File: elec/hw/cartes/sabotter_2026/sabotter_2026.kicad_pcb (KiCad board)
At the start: 2 copper layers, 105 x 80 mm, 131 parts, among them J10 2-1445055-3, J11 3-794618-6, J12 22053031, J13 3-794618-6, J3 USB4105-GF-A-060, J5 2-1445055-4, J6 794618-4, J7 A3C-16DA-2DSC71, J8 A3C-16DA-2DSC71, J9 794618-4, SW1 TSB001A3526A02, U1 OKI-78SR-3.3/1.5-W36H-C, U2 OKI-78SR-5/1.5-W36H-C, U3 ESP32-S3-WROOM-1, U4 ADXRS453BRGZ, U5 SCH16T-K01-10, U6 TCAN1042DRQ1, U7 TCA6408ARGTR, U8 SN74LVC1T45DBV

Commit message: switchs added to motor ribbon cable
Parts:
- added R59: 0R, cocotter_resistor:r0603_reflow, F.Cu at (88.2, -19.9)
- added R60: 0R, cocotter_resistor:r0603_reflow, F.Cu at (88.2, -17.5)

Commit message: sabotter wip
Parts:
- removed C11, C13, C14, C18, C20: 1µF 50V, cocotter_capacitors:C_0805_2012Metric
- removed C15, C16, C19: 100nF 50V, cocotter_capacitors:C_0603_1608Metric
- removed C17: 10µF 25V, cocotter_capacitors:C_0805_2012Metric
- removed D5: 1N5819WS, cocotter_diodes:D_SOD-323
- removed H5: MOUNT-PAD-ROUND3.3, cocotter_others:MountingHole_3.2mm_M3_Pad_Via
- removed J7, J8: A3C-16DA-2DSC71, cocotter_connectors:A3C-16DA-2DSC71
- removed L1: 470µH, cocotter_inductors:L_Kyocera_07A7_7.3x6.6mm
- removed R27: 100k, cocotter_resistor:r0603_reflow
- removed R35, R36: 91k 1%, cocotter_resistor:r0603_reflow
- removed R37, R38: 0R, cocotter_resistor:r0603_reflow
- removed TP4, TP5: TestPoint, cocotter_others:testpoint-THT-0.5mm
- removed U4: ADXRS453BRGZ, cocotter_ic:SOIC-16W_7.5x10.3mm_P1.27mm
- removed U5: SCH16T-K01-10, cocotter_ic:SCH16T
- added C30: 100nF 50V, cocotter_capacitors:C_0603_1608Metric, F.Cu at (149.8, 55.8)
- added J17: 22272061, cocotter_connectors:22272061, B.Cu at (150.0, 50.5)
- added J18: ~, cocotter_connectors:188275-4, B.Cu at (124.8, 88.0)
- added R61: 0R, cocotter_resistor:r0603_reflow, F.Cu at (143.8, 55.8)
- added R62: 91k 1%, cocotter_resistor:r0603_reflow, F.Cu at (157.5, 97.5)
- added R63: 91k 1%, cocotter_resistor:r0603_reflow, F.Cu at (154.4, 97.5)
- added R64: 91k 1%, cocotter_resistor:r0603_reflow, F.Cu at (144.8, 48.0)
- added R65: 0R, cocotter_resistor:r0603_reflow, F.Cu at (167.2, 67.5)
- added TP7: TestPoint, cocotter_others:testpoint-THT-0.5mm, F.Cu at (151.8, 54.5)
- added TP8: TestPoint, cocotter_others:testpoint-THT-0.5mm, F.Cu at (151.8, 56.5)
- added U9: ~, cocotter_ic:OLED_0.96inch, F.Cu at (150.0, 72.0)
- J1: value ~ -> 22272021; moved to B.Cu
- J10: value 2-1445055-3 -> 2-1445051-3; footprint cocotter_connectors:2-1445055-3 -> cocotter_connectors:2-1445051-3; moved to B.Cu
- J11: value 3-794618-6 -> 22272051; footprint cocotter_connectors:3-794618-6 -> cocotter_connectors:22272051; moved to B.Cu
- J12: value 22053031 -> 22272031; footprint cocotter_connectors:22053031 -> cocotter_connectors:22272031; moved to B.Cu
- J13: value 3-794618-6 -> 3-794630-6; footprint cocotter_connectors:3-794618-6 -> cocotter_connectors:3-794630-6; moved to B.Cu
- J15, J16, J4: moved to B.Cu
- J3: value USB4105-GF-A-060 -> USB4120-03-C; footprint cocotter_connectors:USB4105 -> cocotter_connectors:USB4120-03-C
- J5: value 2-1445055-4 -> 22272041; footprint cocotter_connectors:2-1445055-4 -> cocotter_connectors:22272041; moved to B.Cu
- J6, J9: value 794618-4 -> 3-794630-4; footprint cocotter_connectors:798618-4 -> cocotter_connectors:3-794630-4; moved to B.Cu
- R54: value 91k 1% -> 0R
- R55: value 0R -> 91k 1%
- R57: value 91k 1% -> 1k 1%
- R58: value 1k 1% -> 0R
- SW1: value TSB001A3526A02 -> PTS525 SK15 SMTR2 LFS; footprint cocotter_others:TSB001A3526A02 -> cocotter_others:PTS525 SK15 SMTR2 LFS
- moved C25 229.9 mm to (173.0, 108.0), turned to -90 degrees
- moved C26 225.4 mm to (168.5, 108.0), turned to -90 degrees
- moved TP6 217.4 mm to (170.0, 96.5)
- moved U7 213.5 mm to (166.1, 94.8)
- moved R55 208.6 mm to (114.0, 109.0), turned to 180 degrees
- moved R56 203.1 mm to (117.0, 104.5)
- moved U8 199.3 mm to (118.0, 107.0)
- moved R49 185.1 mm to (171.5, 108.0), turned to 90 degrees
- moved U6 184.7 mm to (138.8, 95.9)
- moved R12 176.7 mm to (154.8, 56.5), turned to 180 degrees
- moved C1 174.1 mm to (115.0, 78.0), turned to -90 degrees
- moved R54 172.1 mm to (127.8, 100.2), turned to -90 degrees
- moved R9 170.7 mm to (150.8, 95.0), turned to 180 degrees
- moved R5 168.5 mm to (150.8, 97.0), turned to 180 degrees
- moved R10 167.8 mm to (147.8, 95.0), turned to 180 degrees
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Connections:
- net /motors/MOSI_MOT_3V3 renamed /motors/irq1_3v3
- J11 pad 2: +3V3 -> /interfaces/scl_3v3
- J11 pad 3: /interfaces/scl_3v3 -> /interfaces/sda_3v3
- J11 pad 4: Net-(J11-Pad4) -> +3V3
- J11 pad 5: /interfaces/sda_3v3 -> Net-(J11-Pad5)
- J13 pad 2: +3V3 -> /scl_tof_3v3
- J13 pad 3: /uc/scl_tof_3v3 -> /sda_tof_3v3
- J13 pad 4: /interfaces/enable_tof_3v3 -> +3V3
- J13 pad 5: /uc/sda_tof_3v3 -> /interfaces/enable_tof_3v3
- J14 pad 13: /motors/MISO_MOT_3V3 -> /motors/irq0_3v3
- J14 pad 15: /motors/SCK_MOT_3V3 -> /sda_tof_3v3
- J14 pad 16: /motors//CS_MOT0_3V3 -> /scl_tof_3v3
- J15 pad 13: /motors/MISO_MOT_3V3 -> /motors/irq0_3v3
- J15 pad 15: /motors/SCK_MOT_3V3 -> /sda_tof_3v3
- J15 pad 16: /motors//CS_MOT1_3V3 -> /scl_tof_3v3
- J16 pad 13: /motors/MISO_MOT_3V3 -> /motors/irq0_3v3
- J16 pad 15: /motors/SCK_MOT_3V3 -> /sda_tof_3v3
- J16 pad 16: /motors//CS_MOT2_3V3 -> /scl_tof_3v3
- R10 pad 2: /uc/sda_tof_3v3 -> /sda_tof_3v3
- R50 pad 2: /interfaces/ctc_left_3v3 -> Net-(U7-~{RESET})
- R51 pad 2: Net-(U7-~{RESET}) -> /interfaces/ctc_left_3v3
- R54 pad 1: /interfaces/ws2812_data_3v3 -> +5V
- R54 pad 2: GND -> Net-(J11-Pad5)
- R55 pad 1: +3V3 -> /interfaces/ws2812_data_3v3
- R55 pad 2: Net-(U8-DIR) -> GND
- R56 pad 1: +5V -> +3V3
- R56 pad 2: Net-(J11-Pad6) -> Net-(U8-DIR)
- R57 pad 1: +3V3 -> /interfaces/led_com_3v3
- R57 pad 2: Net-(J11-Pad4) -> Net-(D6-PadA)
- R58 pad 1: /interfaces/led_com_3v3 -> GND
- R58 pad 2: Net-(D6-PadA) -> Net-(U9-GND)
- R59 pad 1: /motors/MISO_MOT_3V3 -> Net-(U9-VCC)
- R59 pad 2: /motors/ctc_right_3v3 -> GND
- R6 pad 2: /uc/scl_tof_3v3 -> /scl_tof_3v3
- R60 pad 1: /motors/SCK_MOT_3V3 -> Net-(U9-VCC)
- R60 pad 2: /motors/ctc_left_3v3 -> +3V3
- TP1 pad 1: /uc/sda_tof_3v3 -> /sda_tof_3v3
- TP2 pad 1: /uc/scl_tof_3v3 -> /scl_tof_3v3
- U3 pad 10: /uc/sda_tof_3v3 -> /sda_tof_3v3
- U3 pad 11: /uc/scl_tof_3v3 -> /scl_tof_3v3
- U6 pad 1: (no net) -> /interfaces/can_tx_3v3
- U7 pad 4: /interfaces/ctc_right_3v3 -> /interfaces/enable_tof_3v3
- U7 pad 5: /interfaces/ctc_left_3v3 -> /interfaces/reset_tof_3v3
- U7 pad 7: /interfaces/reset_tof_3v3 -> /brake_mot_3v3
- U7 pad 8: /interfaces/enable_tof_3v3 -> /interfaces/ctc_left_3v3
- U7 pad 9: /brake_mot_3v3 -> /interfaces/ctc_right_3v3
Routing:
- net /interfaces/scl_3v3: track 0.00 -> 82.9 mm, vias 0 -> 1
- net /interfaces/sda_3v3: track 0.00 -> 78.7 mm, vias 0 -> 2
- net GND: track 0.00 -> 71.9 mm, vias 0 -> 18
- net /uc/USB_D-: track 0.00 -> 51.1 mm, vias 0 -> 2
- net /uc/EN_ESP32_3v3: track 0.00 -> 46.8 mm, vias 0 -> 2
- net /uc/USB_D+: track 0.00 -> 46.8 mm, vias 0 -> 2
- net +3V3: track 0.00 -> 38.5 mm, vias 0 -> 9
- net /uc/esp32_dbg_tx_3v3: track 0.00 -> 36.6 mm
- net /uc/boot/dl_select_3v3: track 0.00 -> 30.9 mm
- net /interfaces/CAN_H: track 0.00 -> 29.8 mm
- net /sensors/lidar_tx_3v3: track 0.00 -> 29.4 mm, vias 0 -> 1
- net /interfaces/CAN_L: track 0.00 -> 29.0 mm
- net /uc/esp32_dbg_rx_3v3: track 0.00 -> 27.5 mm
- net /brake_mot_3v3: track 0.00 -> 21.9 mm, vias 0 -> 1
- net /motors/ENCODER_A_MOT1_3V3: track 0.00 -> 20.6 mm, vias 0 -> 1
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- added copper zone on In1.Cu, net GND
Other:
- board size 105 x 80 mm -> 65 x 100 mm
- copper layers 2 -> 4

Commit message: sabotter wip
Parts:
- moved TP6 67.2 mm to (117.5, 54.5)
- moved D2 66.9 mm to (112.5, 60.0)
- moved R1 63.3 mm to (114.5, 60.0)
- moved D6 63.1 mm to (112.5, 55.5)
- moved SW1 63.1 mm to (115.0, 34.0), turned to 90 degrees
- moved D4 61.0 mm to (112.5, 51.0)
- moved R57 59.3 mm to (114.5, 55.5)
- moved R31 58.3 mm to (173.5, 36.5)
- moved R4 57.0 mm to (114.5, 51.0)
- moved J3 56.9 mm to (115.0, 44.0)
- moved C24 56.8 mm to (169.6, 78.2)
- moved R65 56.2 mm to (120.0, 37.0), turned to 0 degrees
- moved J6 55.4 mm to (169.0, 74.0)
- moved C12 55.2 mm to (167.0, 30.8), turned to 0 degrees
- moved C22 54.6 mm to (169.0, 69.8)
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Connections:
- J13 pad 2: /scl_tof_3v3 -> /sda_tof_3v3
- J13 pad 3: /sda_tof_3v3 -> /scl_tof_3v3
- J5 pad 1: GND -> /sensors/lidar_rx_3v3
- J5 pad 3: /sensors/lidar_tx_3v3 -> GND
- R31 pad 2: /sensors/lidar_tx_3v3 -> /sensors/lidar_rx_3v3
- U3 pad 15: /sensors/lidar_pwm_3v3 -> /motors/ENCODER_B_MOT1_3V3
- U3 pad 17: /interfaces/sda_3v3 -> /motors/ENCODER_B_MOT0_3V3
- U3 pad 18: /interfaces/scl_3v3 -> /motors/ENCODER_A_MOT1_3V3
- U3 pad 28: /sensors/gyro_miso_3v3 -> /motors/ENCODER_A_MOT0_3V3
- U3 pad 29: /sensors/gyro_mosi_3v3 -> /sensors//gyro_cs_3v3
- U3 pad 30: /sensors//gyro_cs_3v3 -> /sensors/gyro_miso_3v3
- U3 pad 31: /sensors/gyro_sck_3v3 -> /sensors/gyro_mosi_3v3
- U3 pad 32: /motors/ENCODER_A_MOT0_3V3 -> /sensors/gyro_sck_3v3
- U3 pad 33: /motors/ENCODER_B_MOT0_3V3 -> /interfaces/sda_3v3
- U3 pad 34: /motors/ENCODER_A_MOT1_3V3 -> /interfaces/scl_3v3
- U3 pad 35: /motors/ENCODER_B_MOT1_3V3 -> /sensors/lidar_pwm_3v3
- U3 pad 38: /sensors/lidar_tx_3v3 -> /sensors/lidar_rx_3v3
- U3 pad 4: /interfaces/tx_to_prop_3v3 -> /interfaces/ws2812_data_3v3
- U3 pad 6: /interfaces/ws2812_data_3v3 -> /interfaces/tx_to_prop_3v3
- U7 pad 10: /interfaces/led_com_3v3 -> /interfaces/color_select_3v3
- U7 pad 2: /interfaces/starting_cord_3v3 -> /interfaces/led_com_3v3
- U7 pad 3: /interfaces/color_select_3v3 -> /interfaces/enable_tof_3v3
- U7 pad 4: /interfaces/enable_tof_3v3 -> /interfaces/reset_tof_3v3
- U7 pad 5: /interfaces/reset_tof_3v3 -> /brake_mot_3v3
- U7 pad 7: /brake_mot_3v3 -> /interfaces/ctc_left_3v3
- U7 pad 8: /interfaces/ctc_left_3v3 -> /interfaces/ctc_right_3v3
- U7 pad 9: /interfaces/ctc_right_3v3 -> /interfaces/starting_cord_3v3
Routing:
- net /interfaces/ws2812_data_3v3: track 2.92 -> 98.9 mm, vias 0 -> 2
- net /interfaces/rx_from_prop_3v3: track 0.00 -> 79.3 mm, vias 0 -> 2
- net GND: track 71.9 -> 141.0 mm, vias 18 -> 37
- net /interfaces/tx_to_prop_3v3: track 0.00 -> 68.3 mm, vias 0 -> 2
- net /sda_tof_3v3: track 0.00 -> 62.0 mm, vias 0 -> 2
- net +5V: track 10.0 -> 69.2 mm, vias 2 -> 7
- net /scl_tof_3v3: track 3.01 -> 61.7 mm, vias 1 -> 2
- net /sensors/lidar_rx_3v3: track 0.00 -> 51.2 mm, vias 0 -> 1
- net /motors/irq0_3v3: track 0.00 -> 45.8 mm, vias 0 -> 3
- net /motors/irq1_3v3: track 0.00 -> 34.1 mm, vias 0 -> 2
- net /brake_mot_3v3: track 21.9 -> 54.5 mm, vias 1 -> 2
- net /sensors/gyro_miso_3v3: track 3.81 -> 34.9 mm
- net /sensors/lidar_tx_3v3: track 29.4 -> 0.00 mm, vias 1 -> 0
- net /sensors//gyro_cs_3v3: track 6.58 -> 35.3 mm
- net /motors/PWM_MOT2_3V3: track 0.00 -> 28.1 mm
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- added copper zone on In2.Cu, net +5V

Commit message: sabotter ready for first schematic and routing review
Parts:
- moved TP2 22.7 mm to (151.5, 44.8)
- moved TP1 21.6 mm to (149.2, 44.8)
- moved R5 4.61 mm to (151.8, 92.5), turned to -90 degrees
- moved R6 4.27 mm to (151.8, 95.5), turned to -90 degrees
- moved R29 3.64 mm to (123.2, 28.0), turned to 90 degrees
- moved R33 3.51 mm to (121.8, 28.0), turned to 90 degrees
- moved R28 2.69 mm to (123.2, 24.0), turned to -90 degrees
- moved R9 2.69 mm to (149.8, 92.5), turned to -90 degrees
- moved R30 2.51 mm to (121.8, 24.0), turned to -90 degrees
- moved R10 2.06 mm to (149.8, 95.5), turned to -90 degrees
- moved R54 1.13 mm to (127.0, 101.0), turned to 0 degrees
- moved R14 1.00 mm to (159.8, 43.5)
- moved R15 1.00 mm to (159.8, 45.0)
- moved C26 0.75 mm to (167.8, 108.0)
- moved R51 0.75 mm to (169.2, 108.0)
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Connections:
- R28 pad 2: /sensors/lidar_tx_3v3 -> /sensors/lidar_pwm_3v3
- R29 pad 2: /sensors/lidar_pwm_3v3 -> /sensors/lidar_rx_3v3
- R30 pad 2: /sensors/lidar_tx_3v3 -> /sensors/lidar_pwm_3v3
- R33 pad 2: /sensors/lidar_pwm_3v3 -> /sensors/lidar_rx_3v3
- U3 pad 10: /sda_tof_3v3 -> /motors/PWM_MOT0_3V3
- U3 pad 11: /scl_tof_3v3 -> /motors/DIR_MOT0_3V3
- U3 pad 12: /interfaces/can_tx_3v3 -> /motors/DIR_MOT1_3V3
- U3 pad 15: /motors/ENCODER_B_MOT1_3V3 -> /motors/PWM_MOT1_3V3
- U3 pad 17: /motors/ENCODER_B_MOT0_3V3 -> /interfaces/can_tx_3v3
- U3 pad 18: /motors/ENCODER_A_MOT1_3V3 -> /interfaces/can_rx_3v3
- U3 pad 19: /interfaces/can_rx_3v3 -> /motors/ENCODER_A_MOT0_3V3
- U3 pad 20: /motors/DIR_MOT0_3V3 -> /motors/ENCODER_B_MOT0_3V3
- U3 pad 21: /motors/PWM_MOT0_3V3 -> /motors/ENCODER_B_MOT2_3V3
- U3 pad 22: /motors/DIR_MOT1_3V3 -> /motors/ENCODER_A_MOT2_3V3
- U3 pad 23: /motors/DIR_MOT2_3V3 -> /sda_tof_3v3
- U3 pad 24: /motors/ENCODER_A_MOT2_3V3 -> /scl_tof_3v3
- U3 pad 25: /motors/ENCODER_B_MOT2_3V3 -> /motors/DIR_MOT2_3V3
- U3 pad 28: /motors/ENCODER_A_MOT0_3V3 -> /motors/PWM_MOT2_3V3
- U3 pad 8: /motors/PWM_MOT1_3V3 -> /motors/ENCODER_B_MOT1_3V3
- U3 pad 9: /motors/PWM_MOT2_3V3 -> /motors/ENCODER_A_MOT1_3V3
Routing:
- net +5V: track 69.2 -> 187.4 mm, vias 7 -> 17
- net Net-(D1-K): track 10.9 -> 111.7 mm, vias 0 -> 2
- net /motors/ENCODER_A_MOT1_3V3: track 8.97 -> 91.6 mm, vias 0 -> 1
- net /motors/PWM_MOT0_3V3: track 9.75 -> 91.0 mm, vias 0 -> 2
- net /motors/DIR_MOT1_3V3: track 5.86 -> 86.6 mm, vias 0 -> 1
- net /motors/DIR_MOT0_3V3: track 5.21 -> 85.5 mm, vias 0 -> 2
- net /motors/ENCODER_B_MOT1_3V3: track 12.7 -> 92.2 mm, vias 0 -> 1
- net /sda_tof_3v3: track 62.0 -> 140.7 mm, vias 2 -> 3
- net /scl_tof_3v3: track 61.7 -> 140.4 mm, vias 2 -> 3
- net /motors/PWM_MOT1_3V3: track 10.6 -> 85.4 mm, vias 0 -> 1
- net /interfaces/led_com_3v3: track 0.00 -> 70.0 mm
- net /motors/ENCODER_A_MOT2_3V3: track 14.7 -> 84.5 mm, vias 0 -> 1
- net /motors/ENCODER_B_MOT0_3V3: track 10.5 -> 78.8 mm, vias 0 -> 2
- net /motors/ENCODER_B_MOT2_3V3: track 16.7 -> 82.5 mm, vias 0 -> 1
- net /interfaces/can_rx_3v3: track 3.01 -> 64.5 mm, vias 0 -> 2
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- added copper zone on In2.Cu, net +3V3
- added copper zone on F.Cu, net +5V
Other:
- board text added: "+"
- board text added: "-"
- board text added: "COM"
- board text added: "PW"
- board text added: "RUN"

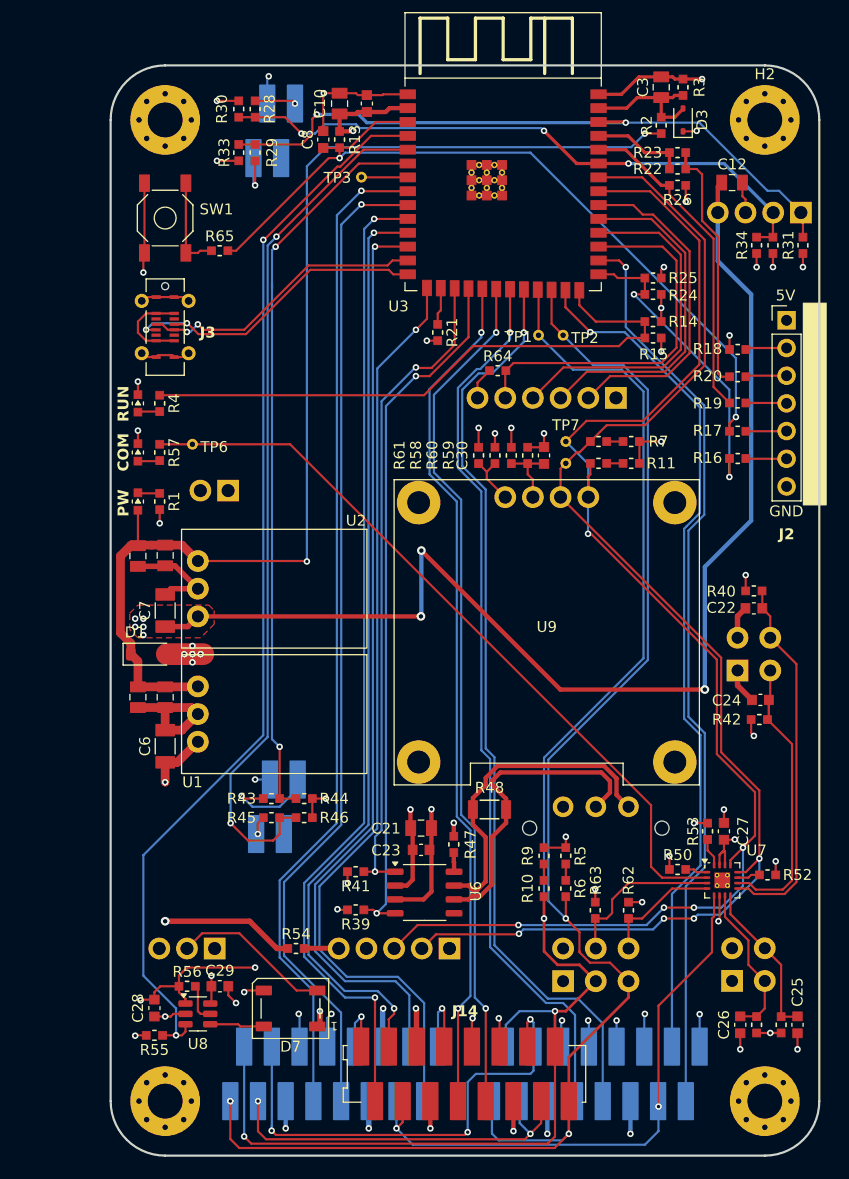
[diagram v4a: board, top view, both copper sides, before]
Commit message: tof irq added, needs routing
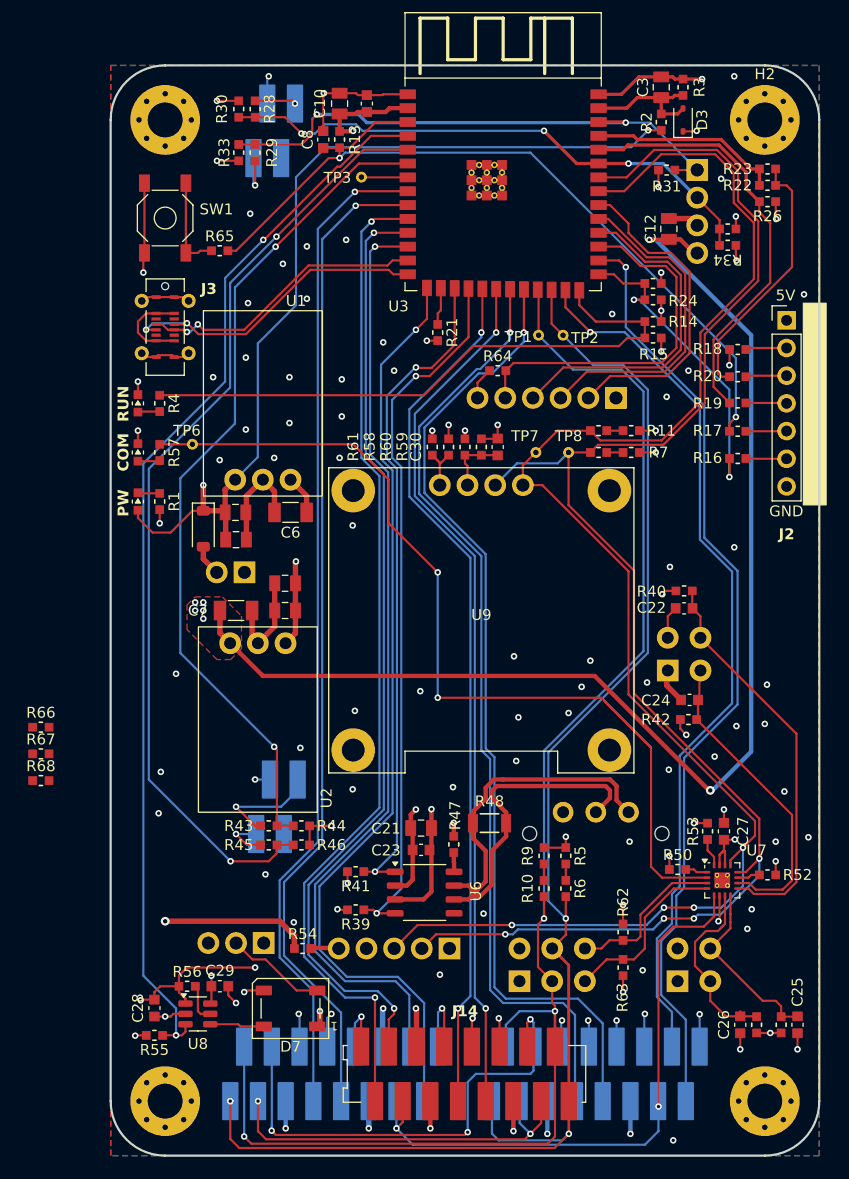
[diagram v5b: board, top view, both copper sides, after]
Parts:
- added R66: 0R, cocotter_resistor:r0603_reflow, F.Cu at (103.6, 80.7)
- added R67: 0R, cocotter_resistor:r0603_reflow, F.Cu at (103.6, 83.2)
- added R68: 91k 1%, cocotter_resistor:r0603_reflow, F.Cu at (103.6, 85.6)
- moved C6 24.3 mm to (126.5, 61.0), turned to 180 degrees
- moved U1 22.3 mm to (124.0, 58.0), turned to 0 degrees
- moved C1 18.1 mm to (121.5, 61.0), turned to 0 degrees
- moved C4 17.0 mm to (121.5, 63.5), turned to 0 degrees
- moved R31 14.3 mm to (161.0, 29.6), turned to 0 degrees
- moved C5 13.7 mm to (126.0, 67.5), turned to 180 degrees
- moved D1 12.5 mm to (118.5, 62.5), turned to -90 degrees
- moved C2 12.1 mm to (126.0, 70.0), turned to 180 degrees
- moved R22 8.39 mm to (170.2, 31.0)
- moved R23 8.39 mm to (170.2, 29.5)
- moved R26 8.39 mm to (170.2, 32.5)
- moved J1 7.65 mm to (121.0, 66.5)
- moved U2 7.43 mm to (123.5, 73.0), turned to 180 degrees
- moved C12 7.19 mm to (161.2, 35.0), turned to 90 degrees
- moved C24 6.50 mm to (163.1, 78.2)
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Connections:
- net Net-(U3-IO7,RTC_GPIO7,GPIO7,TOUCH7,ADC1_CH6) renamed /motors/tof_irq_3v3
- J13 pad 3: /scl_tof_3v3 -> /interfaces/reset_tof_3v3
- J13 pad 5: /interfaces/enable_tof_3v3 -> /scl_tof_3v3
- J13 pad 6: /interfaces/reset_tof_3v3 -> /interfaces/enable_tof_3v3
- R62 pad 1: /interfaces/reset_tof_3v3 -> /interfaces/enable_tof_3v3
- R63 pad 1: /interfaces/enable_tof_3v3 -> /interfaces/reset_tof_3v3
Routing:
- net /interfaces/scl_3v3: track 122.3 -> 142.9 mm
- net +BATT: track 22.2 -> 2.86 mm, vias 5 -> 0
- net /interfaces/led_com_3v3: track 70.0 -> 88.2 mm, vias 0 -> 2
- net /interfaces/sda_3v3: track 125.9 -> 143.4 mm, vias 5 -> 4
- net /sensors/lidar_rx_3v3: track 62.3 -> 50.9 mm
- net /uc/esp32_dbg_rx_3v3: track 30.1 -> 39.6 mm
- net Net-(U3-TXD0,U0TXD,GPIO43,CLK_OUT1): track 8.64 -> 17.5 mm
- net /interfaces/tx_to_prop_3v3: track 68.3 -> 77.2 mm
- net Net-(D1-K): track 111.7 -> 103.3 mm, vias 2 -> 3
- net /interfaces/rx_from_prop_3v3: track 79.3 -> 87.4 mm
- net /sensors/lidar_pwm_3v3: track 57.1 -> 51.0 mm
- net Net-(D7-DOUT): track 14.7 -> 9.25 mm
- net /interfaces/reset_tof_3v3: track 11.1 -> 16.4 mm
- net /motors/ENCODER_B_MOT2_3V3: track 82.5 -> 87.8 mm
- net /motors/ENCODER_A_MOT2_3V3: track 84.5 -> 89.6 mm
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- added copper zone on B.Cu, net GND
- added copper zone on F.Cu, net GND
